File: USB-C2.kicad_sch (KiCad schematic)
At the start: 92 parts, among them J4 USB_C_Receptacle, J5 I2C2_PD_Controller, J6 I2C_Mux, J7 I2C_EEPROM, SW2 FW_Upgrade, U10 24LC256, U11 TPD4E02B04DQA, U12 TPD4E02B04DQA, U13 TPD4E02B04DQA, U14 TUSB1142IRNQR_C5216209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

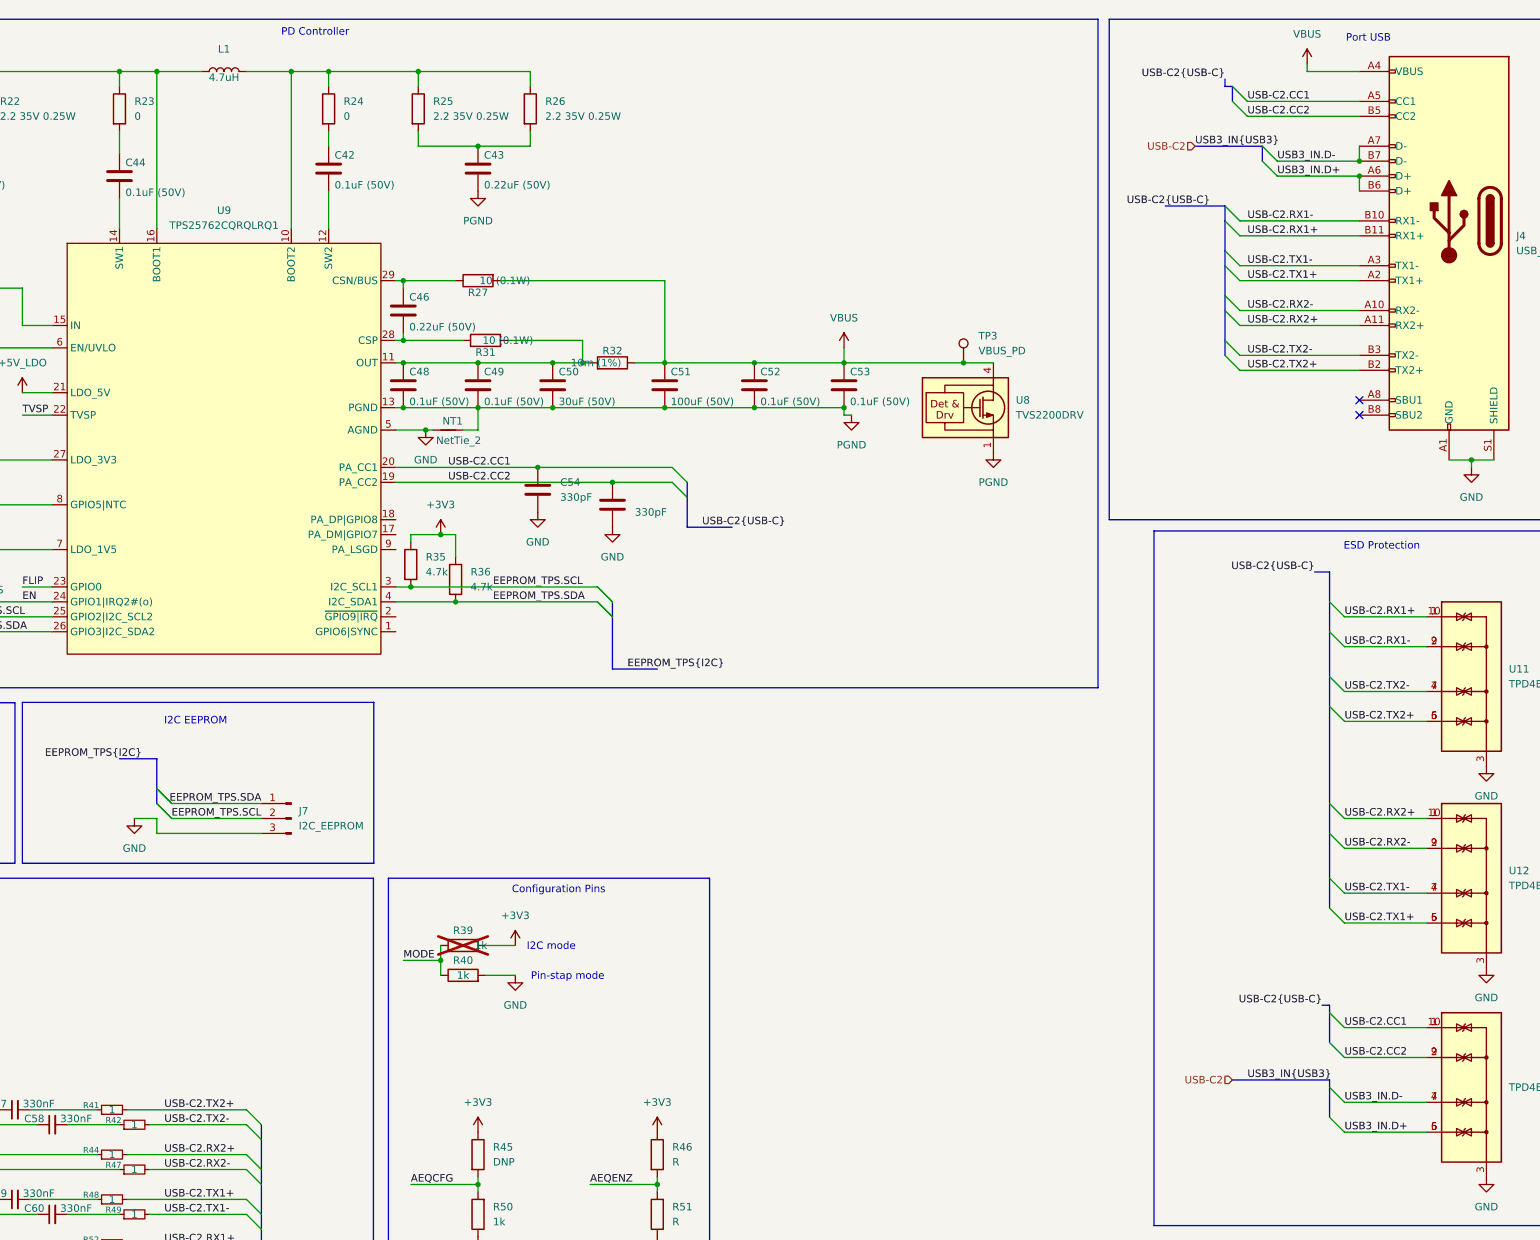
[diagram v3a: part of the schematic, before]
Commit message: minor schematic fixes, footprints changes, layout improvements
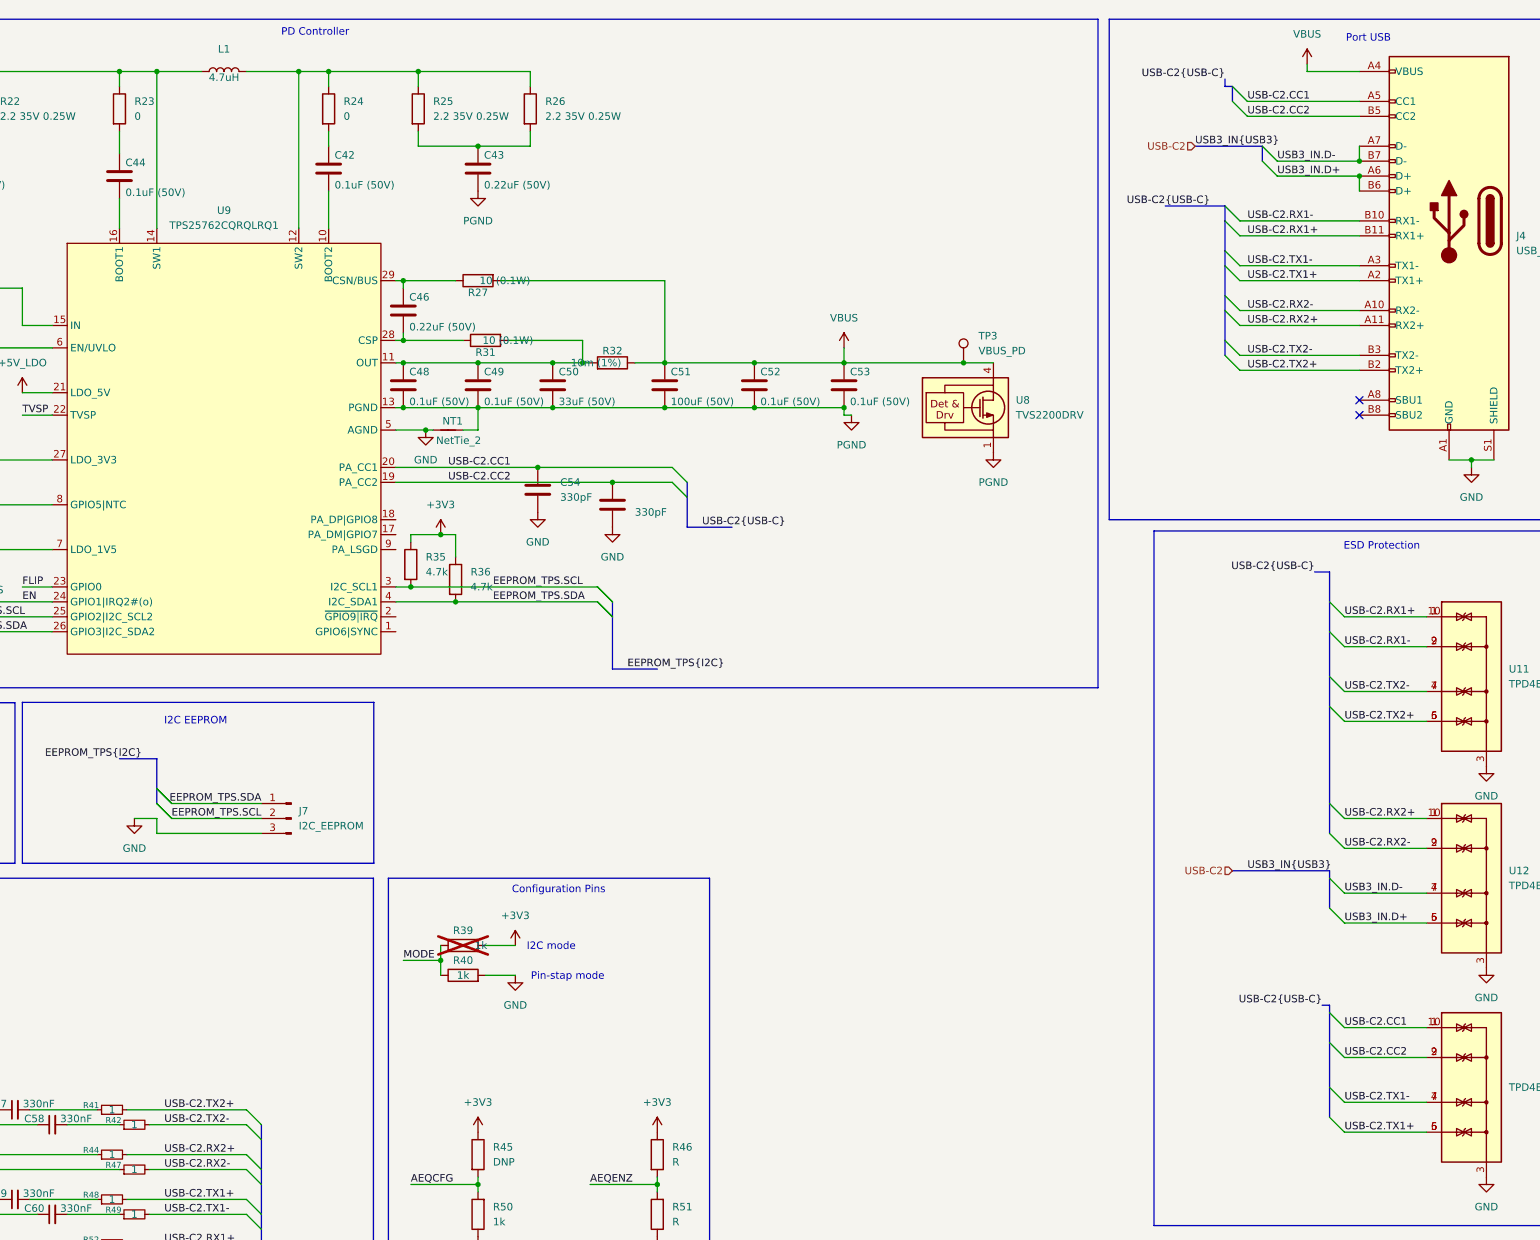
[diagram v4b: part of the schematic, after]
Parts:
- C38: footprint Capacitor_THT:C_Radial_D5.0mm_H11.0mm_P2.00mm -> Capacitor_SMD:C_1812_4532Metric; LCSC Part C88755 -> C141660
- C50: value 30uF (50V) -> 33uF (50V); footprint Capacitor_THT:C_Radial_D5.0mm_H11.0mm_P2.00mm -> Capacitor_SMD:C_2220_5750Metric; LCSC Part C89792 -> C22388553
- SW2: footprint Button_Switch_SMD:SW_Push_1P1T_XKB_TS-1187A -> EasyEDA:ultra_small_switch_1.6x3.0mm
- TP3, TP4: footprint TestPoint:TestPoint_Loop_D1.80mm_Drill1.0mm_Beaded -> TestPoint:TestPoint_Pad_D1.0mm
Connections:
- net USB-C2.TX1+: now also U13.5 (IO4), U13.6 (NC); no longer U12.5 (IO4), U12.6 (NC)
- net USB-C2.TX1-: now also U13.4 (IO3), U13.7 (NC); no longer U12.4 (IO3), U12.7 (NC)
- net USB3_IN.D+: now also U12.5 (IO4), U12.6 (NC); no longer U13.5 (IO4), U13.6 (NC)
- net USB3_IN.D-: now also U12.4 (IO3), U12.7 (NC); no longer U13.4 (IO3), U13.7 (NC)
- net at L1.2, R24.1, R25.1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: now also U9.12 (SW2); no longer U9.10 (BOOT2)
- net at L1.1, R21.1, R22.1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: now also U9.14 (SW1); no longer U9.16 (BOOT1)
- net at C42.2: now also U9.10 (BOOT2); no longer U9.12 (SW2)
- net at C44.2: now also U9.16 (BOOT1); no longer U9.14 (SW1)

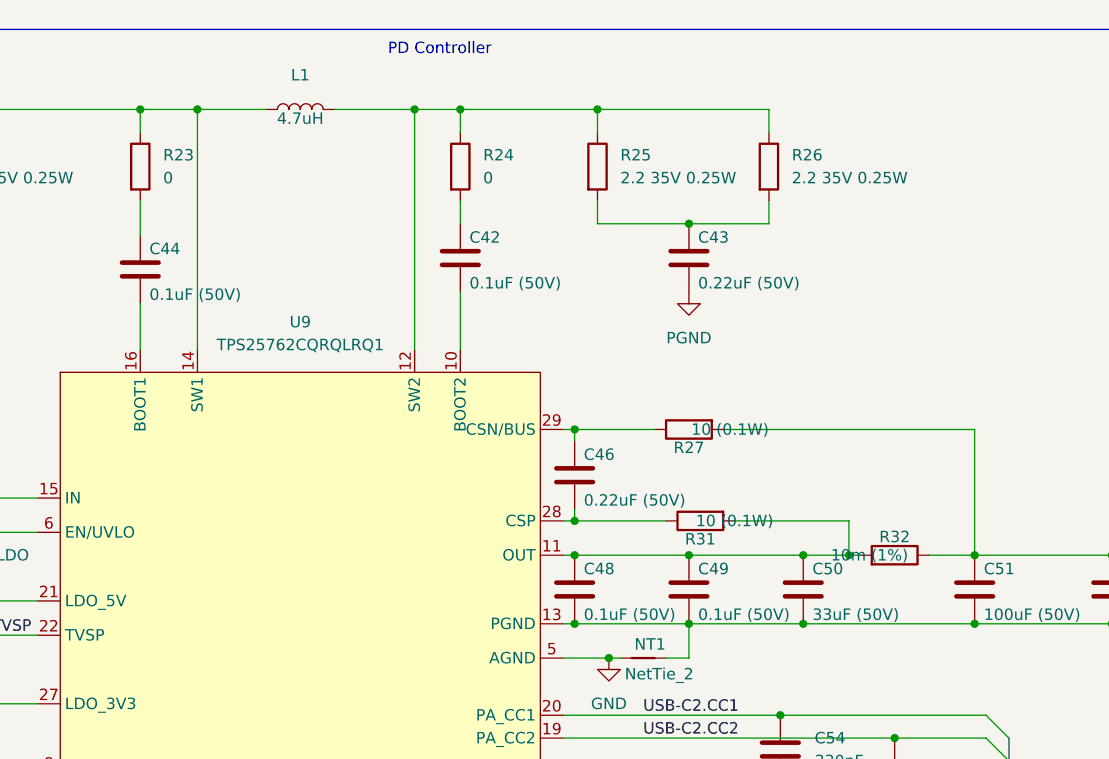
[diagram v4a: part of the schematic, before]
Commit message: comments to schematic added, changed a few components
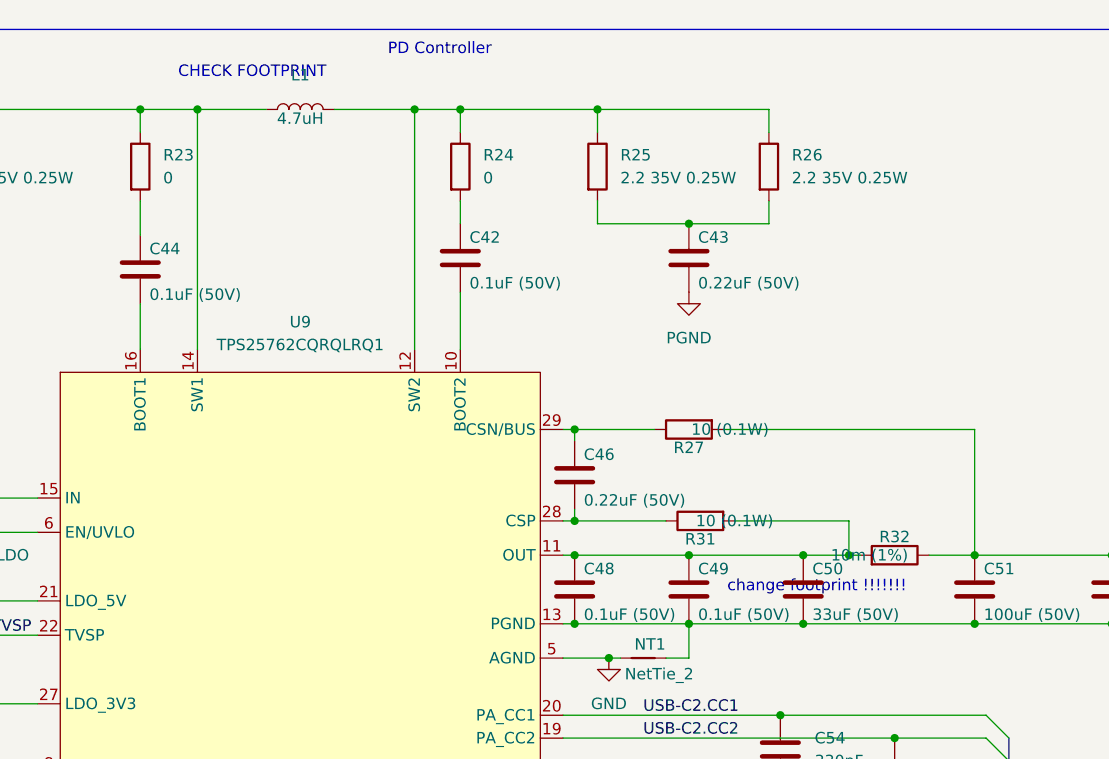
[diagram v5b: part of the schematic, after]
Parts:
- C50: LCSC Part C22388553 -> (none); Mouser Part No  (none) -> 710-865080645010
- J4: Mouser Part No  (none) -> 640-USB4200-03-A
- L1: LCSC Part C19271849 -> C18199458
- R28: Mouser Part No  (none) -> 71-CRCW04026R65FKEDH
- SW2: LCSC Part (none) -> C913788
- U9: Mouser Part No  (none) -> 595-TPS25762CQRQLRQ1
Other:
- note added: "CHECK FOOTPRINT"
- note added: "change footprint !!!!!!!"
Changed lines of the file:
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@@
 		)
 	)
+	(text "CHECK FOOTPRINT\n"
+		(exclude_from_sim no)
+		(at 164.846 18.796 0)
+		(effects
+			(font
+				(size 1.27 1.27)
+			)
+		)
+	)
 	(text "PD Controller"
 		(exclude_from_sim no)
@@
 		)
 	)
+	(text "change footprint !!!!!!!"
+		(exclude_from_sim no)
+		(at 227.584 75.946 0)
+		(effects
+			(font
+				(size 1.27 1.27)
+			)
+		)
+	)
 	(junction
 		(at 382.27 88.9)
@@
 			)
 		)
-		(property "LCSC Part" "C19271849"
+		(property "LCSC Part" "C18199458"
 			(at 170.18 22.86 90)
 			(effects
@@
 			)
 		)
-		(property "LCSC Part" "C22388553 "
+		(property "LCSC Part" ""
+			(at 226.06 76.2 0)
+			(effects
+				(font
+					(size 1.27 1.27)
+				)
+				(hide yes)
+			)
+		)
+		(property "Mouser Part No " "710-865080645010 "
 			(at 226.06 76.2 0)
 			(effects
@@
 			)
 		)
+		(property "Mouser Part No " "640-USB4200-03-A "
+			(at 378.46 48.26 0)
+			(effects
+				(font
+					(size 1.27 1.27)
+				)
+				(hide yes)
+			)
+		)
 		(pin "A6"
 		)
@@
 			)
 		)
+		(property "Mouser Part No " "71-CRCW04026R65FKEDH "
+			(at 21.59 62.23 0)
+			(effects
+				(font
+					(size 1.27 1.27)
+				)
+				(hide yes)
+			)
+		)
 		(pin "1"
 		)
@@
 			)
 		)
+		(property "LCSC Part" "C913788 "
+			(at 21.59 71.12 90)
+			(effects
+				(font
+					(size 1.27 1.27)
+				)
+				(hide yes)
+			)
+		)
 		(pin "2"
 		)
@@
 			(effects
 				(font
+					(size 1.27 1.27)
+				)
+				(hide yes)
+			)
+		)
+		(property "Mouser Part No " "595-TPS25762CQRQLRQ1"
+			(at 170.18 88.9 0)
+			(effects
+				(font

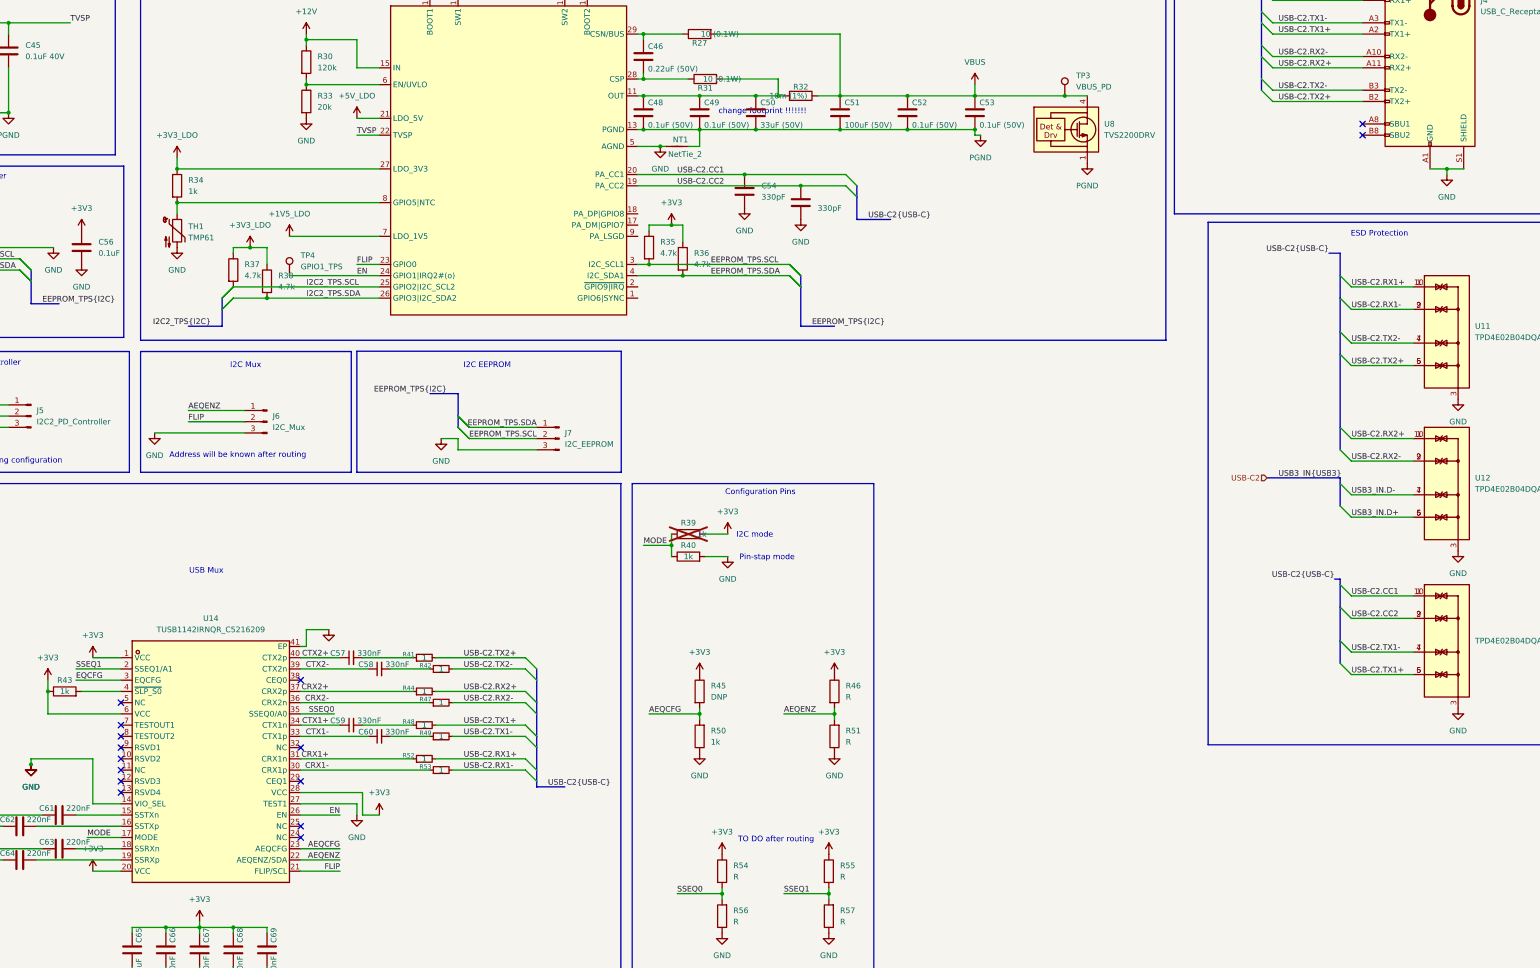
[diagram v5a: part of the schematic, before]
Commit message: Rearrange of the component placement, scheme changes for better routing
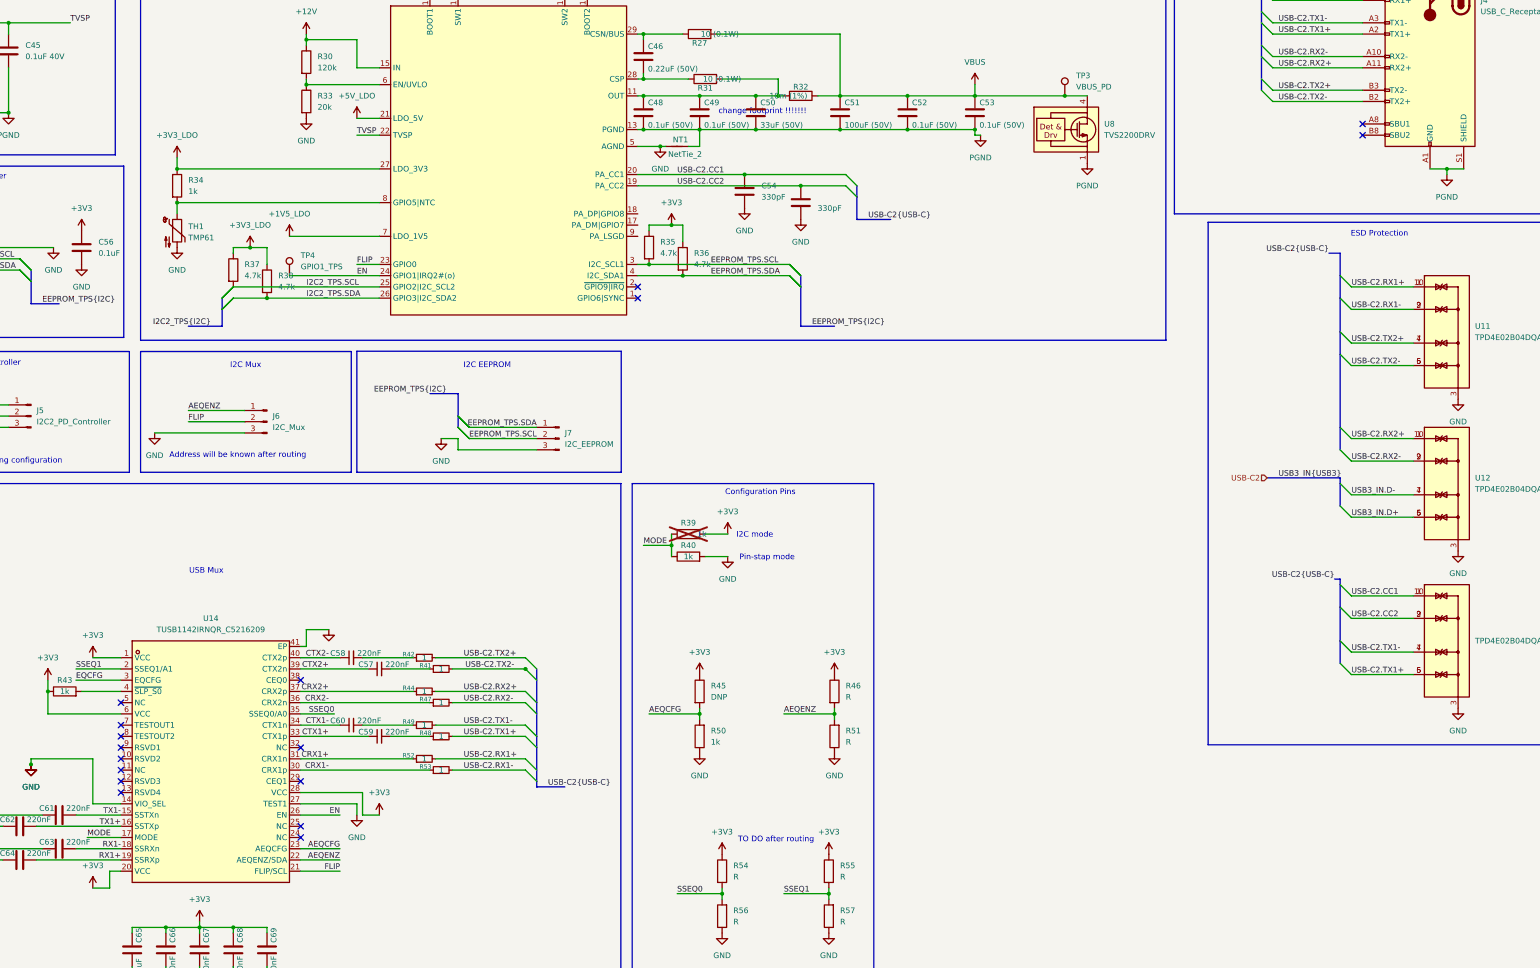
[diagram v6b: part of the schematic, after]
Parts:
- C33, C35, C37, C39, C40, C56, C66, C67, C68, C69: footprint Capacitor_SMD:C_0402_1005Metric -> Capacitor_SMD:C_0201_0603Metric; LCSC Part C5182432 -> C181043
- C57, C58, C59, C60: value 330nF -> 220nF; footprint Capacitor_SMD:C_0402_1005Metric -> Capacitor_SMD:C_0201_0603Metric; LCSC Part C18164591 -> C701263
- C61, C62, C63, C64: footprint Capacitor_SMD:C_0402_1005Metric -> Capacitor_SMD:C_0201_0603Metric; LCSC Part C114401 -> C701263
- J5, J6, J7: footprint Connector_PinHeader_1.27mm:PinHeader_1x02_P1.27mm_Vertical -> Connector_PinHeader_1.00mm:PinHeader_1x03_P1.00mm_Vertical
- R41, R42, R44, R47, R48, R49, R52, R53: footprint Resistor_SMD:R_0402_1005Metric -> Resistor_SMD:R_0201_0603Metric; LCSC Part C185446 -> C469665
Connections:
- net CTX1+: now also U14.33 (CTX1p); no longer U14.34 (CTX1n)
- net CTX1-: now also U14.34 (CTX1n); no longer U14.33 (CTX1p)
- net CTX2+: now also U14.39 (CTX2n); no longer U14.40 (CTX2p)
- net CTX2-: now also U14.40 (CTX2p); no longer U14.39 (CTX2n)
- net GND: no longer J4.A1 (GND), J4.A12 (GND), J4.B1 (GND), J4.B12 (GND), J4.S1 (SHIELD)
- net PGND: now also J4.A1 (GND), J4.A12 (GND), J4.B1 (GND), J4.B12 (GND), J4.S1 (SHIELD)
- net USB-C2.TX2+: now also J4.B3 (TX2-), R42.2, U11.4 (IO3), U11.7 (NC); no longer J4.B2 (TX2+), R41.2, U11.5 (IO4), U11.6 (NC)
- net USB-C2.TX2-: now also J4.B2 (TX2+), R41.2, U11.5 (IO4), U11.6 (NC); no longer J4.B3 (TX2-), R42.2, U11.4 (IO3), U11.7 (NC)
- net RX1+: now reaches C64.2, U14.19 (SSRXp)
- net TX1-: now reaches C61.2, U14.15 (SSTXn)
- net TX1+: now reaches C62.2, U14.16 (SSTXp)
- net RX1-: now reaches C63.2, U14.18 (SSRXn)
- no-connect marks 16 -> 18
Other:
- moved on the sheet: C57, C58, C59, C60, R41, R42, R48, R49
